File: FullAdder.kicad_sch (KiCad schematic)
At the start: 5 parts, among them J1 Conn_01x03, U1 4081, U2 4081, U3 4069, U4 4071

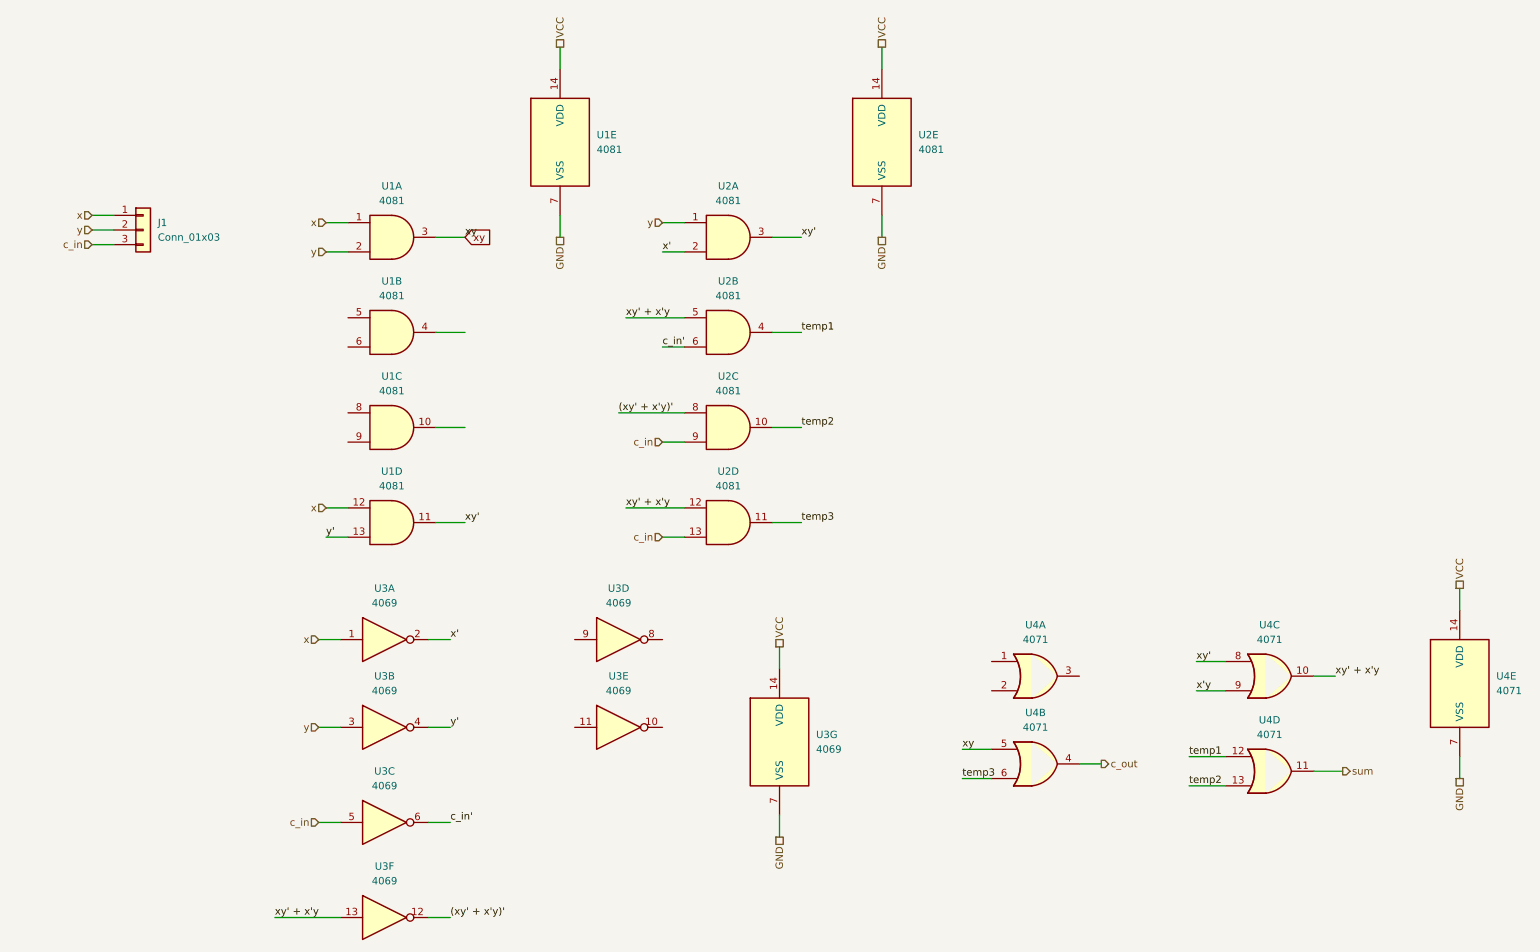
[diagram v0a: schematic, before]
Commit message: Add files via upload
Added 3 bits 2:1 and 6 bits 4:1 multiplexer
Added minus operation
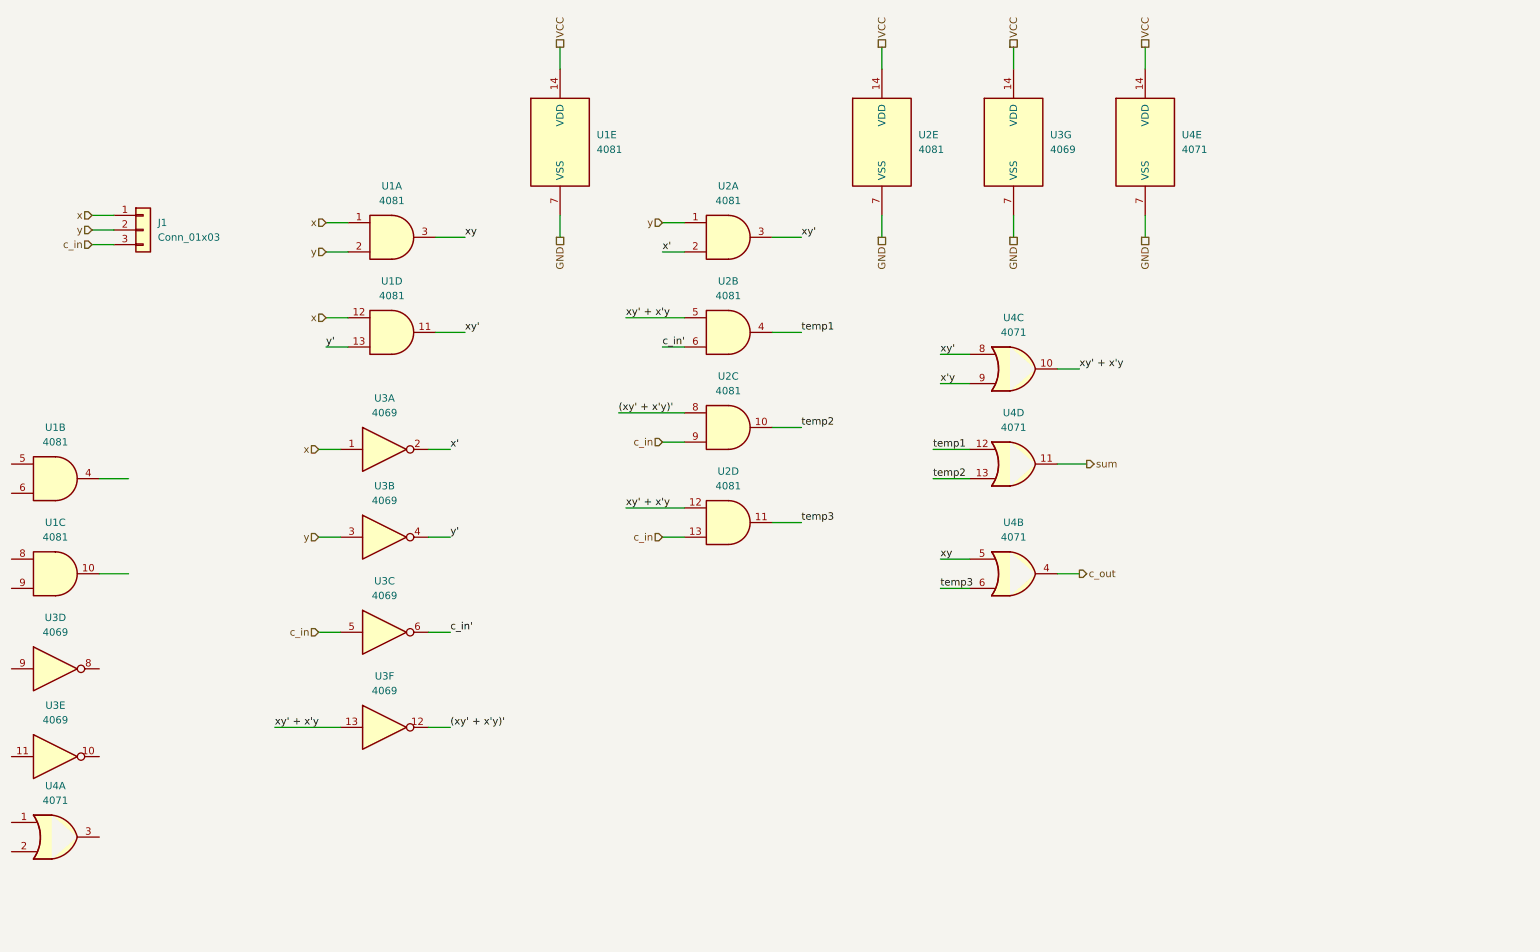
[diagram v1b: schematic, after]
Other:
- moved on the sheet: U1B, U1C, U1D, U3A, U3B, U3C, U3D, U3E, U3F, U3G, U4A, U4B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

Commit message: Add files via upload
Waiting for approval
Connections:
- net xy' + x'y renamed xor_out
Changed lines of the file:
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@@
 	(generator_version "9.0")
 	(paper "A4")
+	(junction
+		(at 74.93 142.24)
+		(diameter 0)
+		(color 0 0 0 0)
+	)
 	(wire
 		(pts
@@
 	(wire
 		(pts
-			(xy 77.47 142.24) (xy 66.04 142.24)
+			(xy 77.47 142.24) (xy 74.93 142.24)
 		)
 		(stroke
@@
 	(wire
 		(pts
+			(xy 74.93 156.21) (xy 92.71 156.21)
+		)
+		(stroke
+			(width 0)
+			(type default)
+		)
+	)
+	(wire
+		(pts
 			(xy 34.29 55.88) (xy 38.1 55.88)
 		)
@@
 	(wire
 		(pts
+			(xy 74.93 142.24) (xy 66.04 142.24)
+		)
+		(stroke
+			(width 0)
+			(type default)
+		)
+	)
+	(wire
+		(pts
 			(xy 74.93 71.12) (xy 78.74 71.12)
+		)
+		(stroke
+			(width 0)
+			(type default)
+		)
+	)
+	(wire
+		(pts
+			(xy 74.93 142.24) (xy 74.93 156.21)
 		)
 		(stroke
@@
 		)
 	)
+	(hierarchical_label "xor_out"
+		(shape output)
+		(at 92.71 156.21 0)
+		(effects
+			(font
+				(size 1.27 1.27)
+			)
+			(justify left)
+		)
+	)

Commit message: Add files via upload
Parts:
- removed J1: Conn_01x03, Connector_PinHeader_2.54mm:PinHeader_1x03_P2.54mm_Vertical, symbol Connector_Generic:Conn_01x03

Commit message: Add files via upload
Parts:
- renumbered U1 to U3, U3 to U4, U4 to U5, U2 to U6
